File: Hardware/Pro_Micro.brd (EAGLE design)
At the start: 17.8 x 33 mm, 33 parts, among them U2 MIC5219, U3 ATMEGA32U4, Y1 16MHz

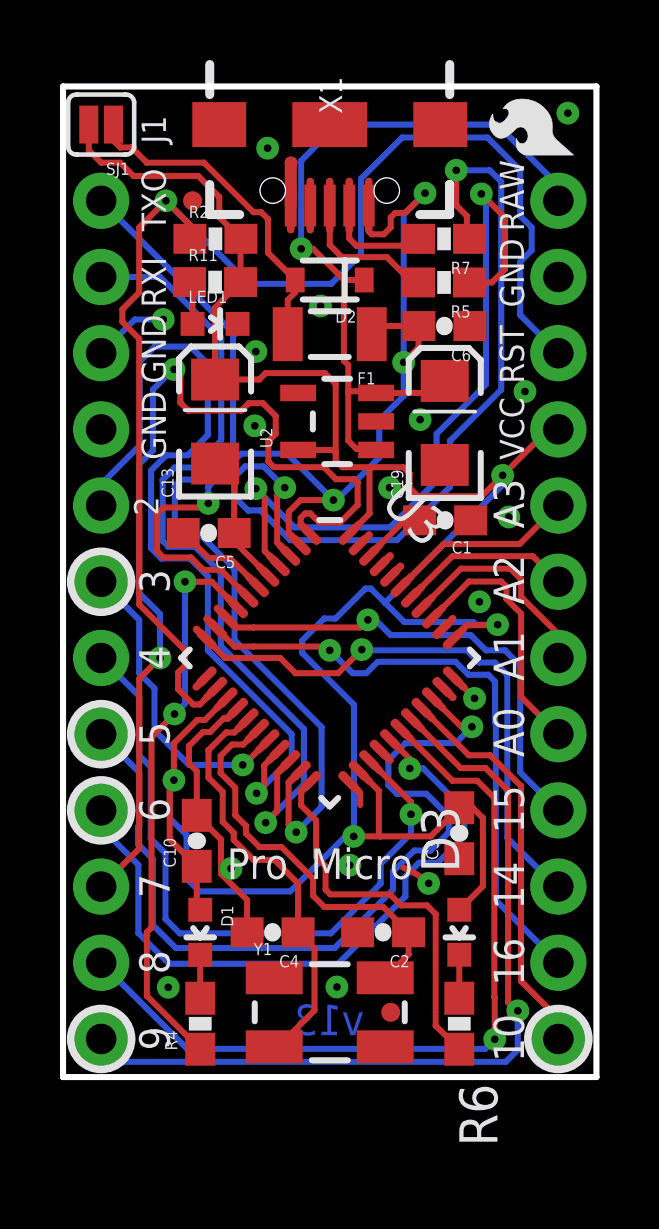
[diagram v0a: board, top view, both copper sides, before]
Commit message: add ignore, moved fiductials and one via
one fid used to be under crystal
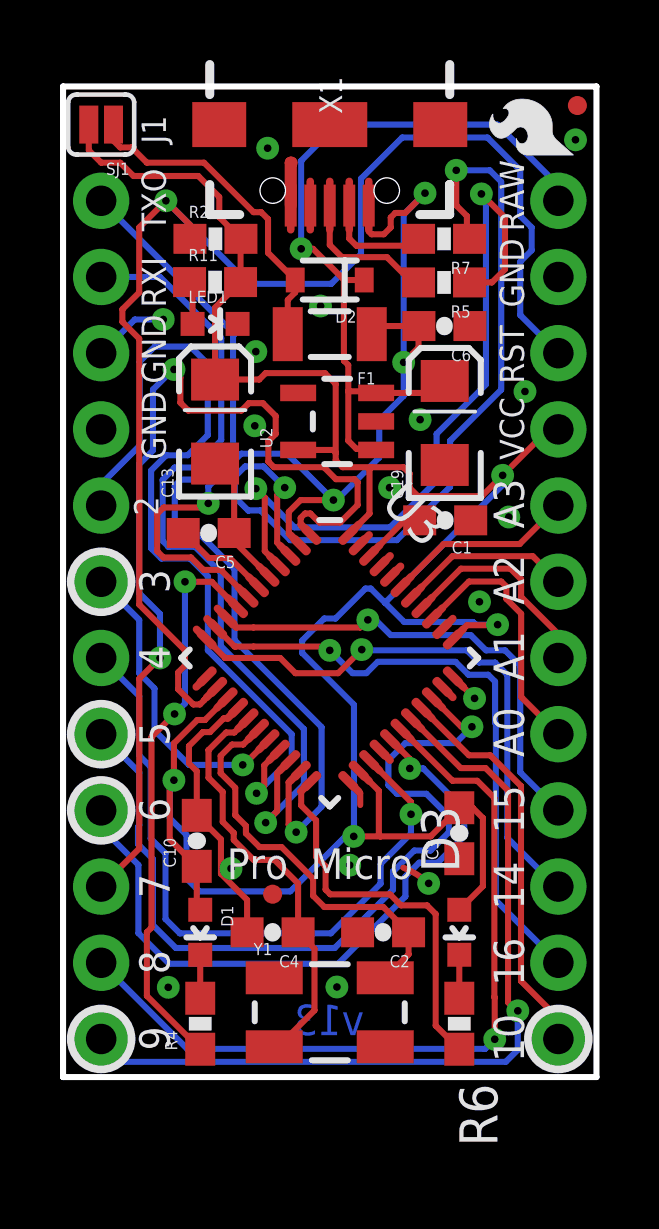
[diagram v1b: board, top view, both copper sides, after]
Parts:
- moved JP2 13.2 mm to (17.1, 32.4)
- moved JP1 5.57 mm to (6.99, 6.10)
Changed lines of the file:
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@@
 <?xml version="1.0" encoding="utf-8"?>
 <!DOCTYPE eagle SYSTEM "eagle.dtd">
-<eagle version="6.4">
+<eagle version="6.5.0">
 <drawing>
 <settings>
@@
 <layer number="29" name="tStop" color="7" fill="3" visible="no" active="yes"/>
 <layer number="30" name="bStop" color="7" fill="6" visible="no" active="yes"/>
-<layer number="31" name="tCream" color="7" fill="4" visible="no" active="yes"/>
+<layer number="31" name="tCream" color="7" fill="4" visible="yes" active="yes"/>
 <layer number="32" name="bCream" color="7" fill="5" visible="no" active="yes"/>
 <layer number="33" name="tFinish" color="6" fill="3" visible="no" active="yes"/>
@@
 <attribute name="VALUE" x="5.461" y="28.448" size="0.762" layer="27" rot="R90"/>
 </element>
-<element name="JP1" library="SparkFun" package="MICRO-FIDUCIAL" value="FIDUCIALUFIDUCIAL" x="10.922" y="2.159"/>
-<element name="JP2" library="SparkFun" package="MICRO-FIDUCIAL" value="FIDUCIALUFIDUCIAL" x="4.318" y="29.21"/>
+<element name="JP1" library="SparkFun" package="MICRO-FIDUCIAL" value="FIDUCIALUFIDUCIAL" x="6.985" y="6.096"/>
+<element name="JP2" library="SparkFun" package="MICRO-FIDUCIAL" value="FIDUCIALUFIDUCIAL" x="17.145" y="32.385"/>
 <element name="F1" library="SparkFun" package="PTC-1206" value="500mA" x="8.89" y="24.765" rot="R180"/>
 <element name="D2" library="SparkFun" package="SOD-323" value="" x="8.89" y="26.5684" rot="R180"/>
@@
 <via x="10.883903125" y="19.646896875" extent="1-16" drill="0.254"/>
 <via x="6.3906375" y="21.70938125" extent="1-16" drill="0.254"/>
-<via x="16.8275" y="32.131" extent="1-16" drill="0.254"/>
+<via x="17.0815" y="31.242" extent="1-16" drill="0.254"/>
 <via x="13.716" y="12.6238" extent="1-16" drill="0.254"/>
 <via x="8.582659375" y="25.702259375" extent="1-16" drill="0.254"/>
